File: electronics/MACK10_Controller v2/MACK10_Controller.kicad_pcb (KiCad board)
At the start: 2 copper layers, 80 x 85.7 mm, 36 parts, among them J1 Motor, J10 I/O, J3 Load Cell, J4 24V IN, J5 SSD1306, J6 INPUT, J7 E_STOP, J8 LIM_TOP, J9 LIM_BOT, U1 U1 ESP32_DEVKIT_30P, U2 HX711, U3 TMC2208, U4 LM2596 Buck Converter

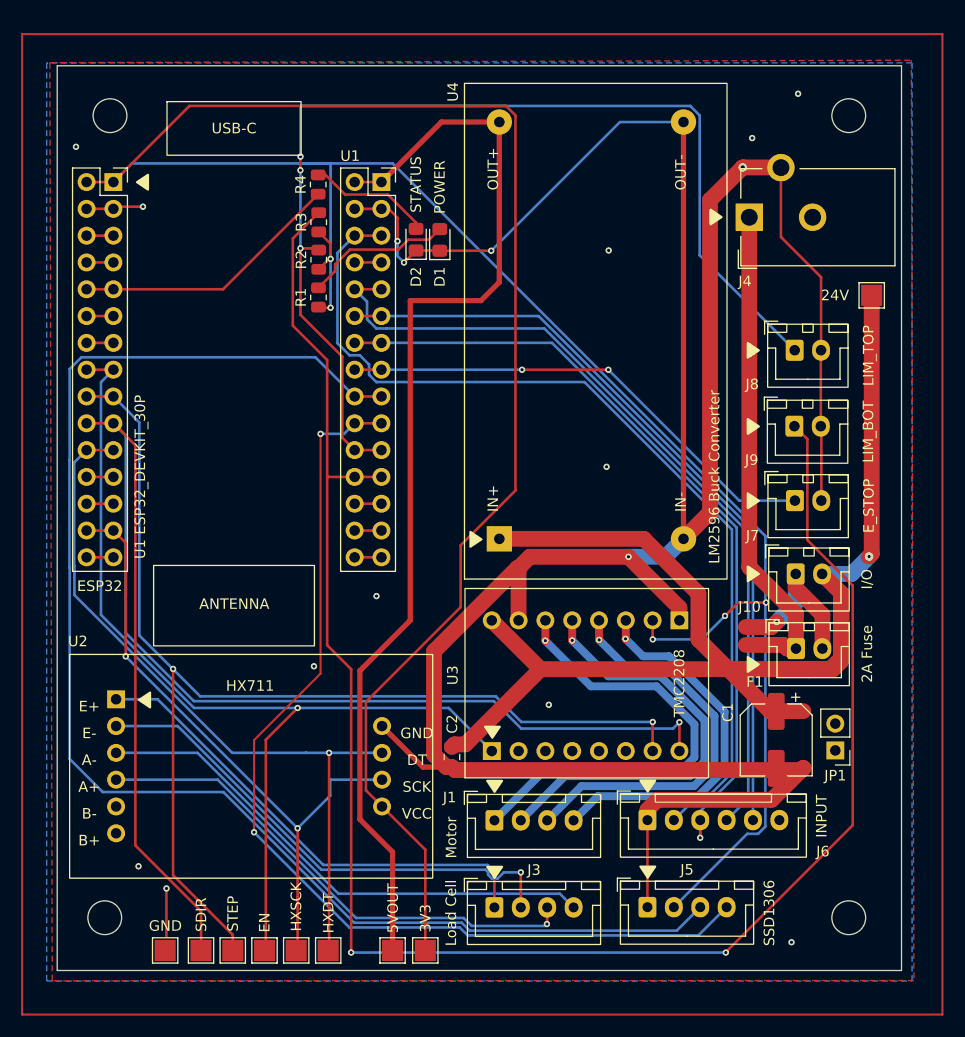
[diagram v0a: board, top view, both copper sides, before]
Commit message: First pass of PCB Layout (front and back)
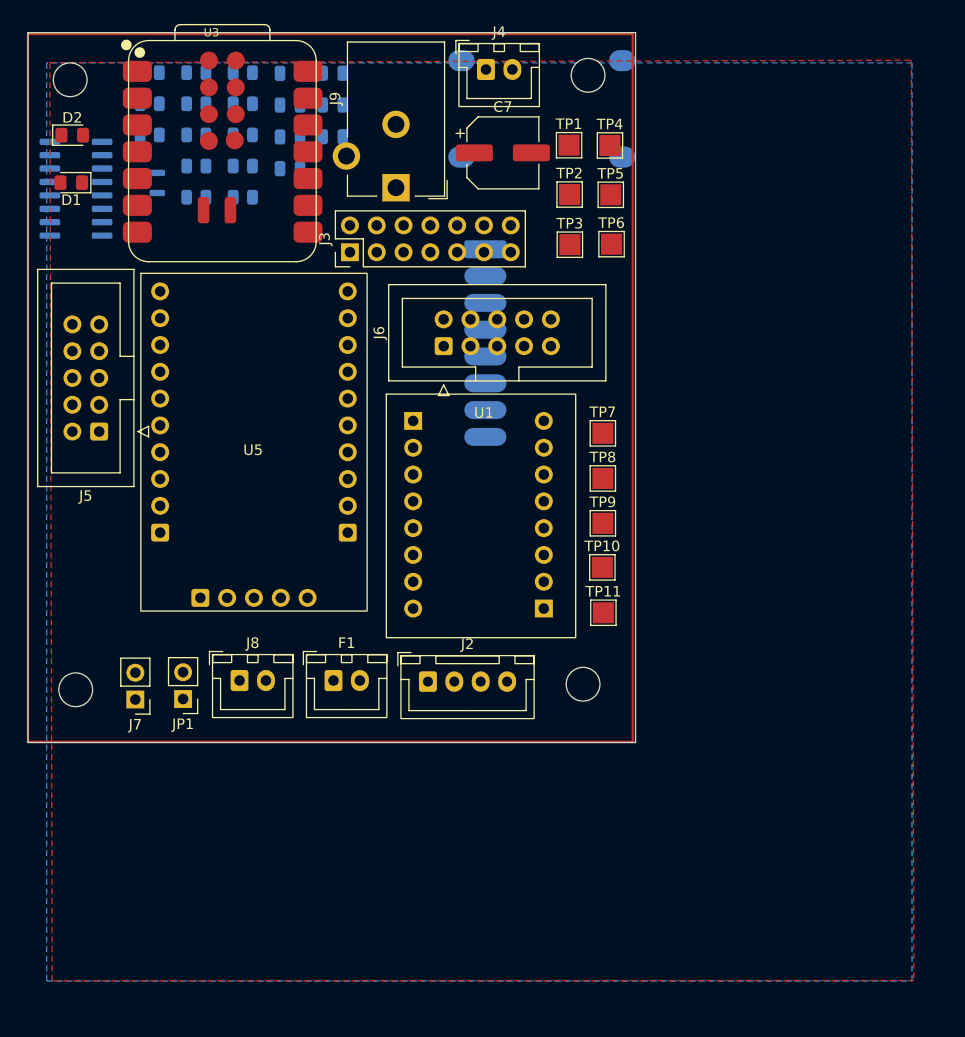
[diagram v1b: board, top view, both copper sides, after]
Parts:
- removed J1: Motor, Connector_JST:JST_XH_B4B-XH-A_1x04_P2.50mm_Vertical
- removed J10: I/O, Connector_JST:JST_XH_B2B-XH-A_1x02_P2.50mm_Vertical
- added C3: 10uF, Capacitor_SMD:C_0805_2012Metric, B.Cu at (42.1, 27.0)
- added C4: 0.1uF, Capacitor_SMD:C_0805_2012Metric, B.Cu at (42.1, 30.0)
- added C5: 100nF 50V, Capacitor_SMD:C_0805_2012Metric, B.Cu at (46.1, 21.0)
- added C6: 0.1uF, Capacitor_SMD:C_0805_2012Metric, B.Cu at (46.1, 24.0)
- added C7: 100uF 35V, Capacitor_SMD:CP_Elec_6.3x7.7, F.Cu at (62.2, 28.5)
- added C8: 0.1uF, Capacitor_SMD:C_0805_2012Metric, B.Cu at (46.1, 27.0)
- added J2: Motor, Connector_JST:JST_XH_B4B-XH-A_1x04_P2.50mm_Vertical, F.Cu at (55.1, 78.6)
- added Q1: SS8550, Package_TO_SOT_SMD:SOT-23, B.Cu at (28.5, 31.4)
- added R10: 10k, Resistor_SMD:R_0805_2012Metric, B.Cu at (33.2, 32.7)
- added R11: 4.7k, DNP, Resistor_SMD:R_0805_2012Metric, B.Cu at (28.8, 20.9)
- added R12: 4.7k, DNP, Resistor_SMD:R_0805_2012Metric, B.Cu at (28.8, 23.9)
- added R13: 10k, Resistor_SMD:R_0805_2012Metric, B.Cu at (28.8, 26.8)
- added R5: 470, Resistor_SMD:R_0805_2012Metric, B.Cu at (37.6, 32.7)
- added R6: 1k, Resistor_SMD:R_0805_2012Metric, B.Cu at (33.2, 20.9)
- added R7: 1k, Resistor_SMD:R_0805_2012Metric, B.Cu at (33.2, 23.9)
- added R8: 10k, Resistor_SMD:R_0805_2012Metric, B.Cu at (33.2, 26.8)
- added R9: 10k, Resistor_SMD:R_0805_2012Metric, B.Cu at (33.2, 29.8)
- added TP10: 5VOUT, TestPoint:TestPoint_Pad_2.0x2.0mm, F.Cu at (71.7, 67.8)
- added TP11: GND, TestPoint:TestPoint_Pad_2.0x2.0mm, F.Cu at (71.8, 72.1)
- added U5: PCF8575, MACK10:PCF8575, F.Cu at (33.6, 70.7)
- added U6: MINI360, Mini360:Mini360_step-down, B.Cu at (65.9, 24.4)
- C1: value 100uF 35V -> 0.1uF; footprint Capacitor_SMD:CP_Elec_6.3x7.7 -> Capacitor_SMD:C_0805_2012Metric; moved to B.Cu
- C2: value 100nF 50V -> 10uF; moved to B.Cu
- D2: value STATUS -> SMD_STATUS
- J3: value Load Cell -> J_Expansion; footprint Connector_JST:JST_XH_B4B-XH-A_1x04_P2.50mm_Vertical -> Connector_PinHeader_2.54mm:PinHeader_2x07_P2.54mm_Vertical
- J4: value 24V IN -> I/O; footprint Connector_BarrelJack:BarrelJack_CUI_PJ-102AH_Horizontal -> Connector_JST:JST_XH_B2B-XH-A_1x02_P2.50mm_Vertical
- J5: value SSD1306 -> Sensor IDC; footprint Connector_JST:JST_XH_B4B-XH-A_1x04_P2.50mm_Vertical -> Connector_IDC:IDC-Header_2x05_P2.54mm_Vertical
- J6: value INPUT -> Interface IDC; footprint Connector_JST:JST_XH_B6B-XH-A_1x06_P2.50mm_Vertical -> Connector_IDC:IDC-Header_2x05_P2.54mm_Vertical
- J7: value E_STOP -> Fan; footprint Connector_JST:JST_XH_B2B-XH-A_1x02_P2.50mm_Vertical -> Connector_PinHeader_2.54mm:PinHeader_1x02_P2.54mm_Vertical
- J8: value LIM_TOP -> E_STOP
- J9: value LIM_BOT -> 24V IN; footprint Connector_JST:JST_XH_B2B-XH-A_1x02_P2.50mm_Vertical -> Connector_BarrelJack:BarrelJack_CUI_PJ-102AH_Horizontal
- R1: value 1k -> 100; moved to B.Cu
- R2: value 10k -> 100; moved to B.Cu
- R3: value 10k -> 18k; moved to B.Cu
- R4: value 1k -> 7.5k; moved to B.Cu
- TP1: value 3V3 -> STEP
- TP2: value HXDT -> HX_DT
- TP3: value 5VOUT -> HX_SCK
- TP4: value GND -> SDA
- TP5: value 24V -> SCL
- TP6: value HXSCK -> VMOT
- TP7: value EN -> M24V
- TP8: value STEP -> 3V3
- TP9: value SDIR -> 24V
- U1: value U1 ESP32_DEVKIT_30P -> TMC2208; footprint MACK10:ESP32_DEVKIT_30PIN -> MACK10:TMC2208_STEPSTICK
- U2: footprint MACK10:HX711_MODULE -> Package_SO:SOIC-16_3.9x9.9mm_P1.27mm; moved to B.Cu
- U3: value TMC2208 -> XIAO-C6; footprint MACK10:TMC2208_STEPSTICK -> XIAO-SEEDSTUDIO:XIAO-ESP32-C6-SMD
- U4: value LM2596 Buck Converter -> INA226; footprint MACK10:LM2596_BUCK_CONVERTER -> MACK10:INA226; moved to B.Cu
- moved TP4 87.1 mm to (72.4, 27.8)
- moved C1 78.2 mm to (42.1, 21.0), turned to 180 degrees
- moved TP1 77.5 mm to (68.5, 27.8), turned to 0 degrees
- moved TP2 75.2 mm to (68.5, 32.5), turned to 0 degrees
- moved TP6 73.3 mm to (72.5, 37.2), turned to 0 degrees
- moved TP3 69.0 mm to (68.6, 37.2), turned to 0 degrees
- moved J5 68.8 mm to (24.0, 54.9), turned to 180 degrees
- moved J7 65.3 mm to (27.4, 80.3), turned to 180 degrees
- moved C2 63.7 mm to (42.1, 24.0), turned to 180 degrees
- moved J3 63.6 mm to (47.7, 37.9), turned to 90 degrees
- moved JP1 62.0 mm to (31.9, 80.3)
- moved J8 61.2 mm to (37.3, 78.5)
- moved TP7 58.6 mm to (71.7, 55.1), turned to 0 degrees
- moved U3 57.7 mm to (26.8, 38.9), turned to 0 degrees
- moved TP8 56.8 mm to (71.7, 59.4), turned to 0 degrees
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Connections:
- C1 pad 1: /+24V -> Net-(U2-INA-)
- C1 pad 2: /GND -> Net-(U2-INA+)
- C2 pad 1: /+24V -> /GND
- C2 pad 2: /GND -> /+5V
- D2 pad 1: /GND -> /STATUS
- J3 pad 1: /LOAD_E+ -> /GND
- J3 pad 2: /LOAD_E- -> /GND
- J3 pad 3: /LOAD_A+ -> /3V3
- J3 pad 4: /LOAD_A- -> /IO3
- J4 pad 1: /24VIN -> Net-(F1-Pin_2)
- J4 pad 2: unconnected-(J4-Pin_2-Pad2) -> /+24V
- J5 pad 1: /GND -> /E_STOP_SENSE
- J5 pad 2: /3V3 -> /GND
- J5 pad 3: /ESP32 D33 -> /LIM_BOT
- J5 pad 4: /ESP32 D32 -> /GND
- J6 pad 1: /GND -> /RIGHT
- J6 pad 2: /UP -> /LEFT
- J6 pad 3: /DOWN -> /UP
- J6 pad 4: /SELECT -> /DOWN
- J6 pad 5: /BACK -> /+5V
- J6 pad 6: unconnected-(J6-Pin_6-Pad6) -> /USER_LED
- J7 pad 1: /ESP32 D25 -> /+5V
- J8 pad 1: /ESP32 D35 -> /+24V
- J8 pad 2: /GND -> /MOTOR_24V
- J9 pad 1: /ESP32 D34 -> /24VIN
- R1 pad 1: /3V3 -> Net-(J1-A-)
- R1 pad 2: Net-(D1-A) -> Net-(U2-INA-)
- R2 pad 1: /3V3 -> Net-(J1-E-)
- R2 pad 2: /ESP32 D35 -> Net-(U2-INA+)
- R3 pad 1: /3V3 -> Net-(U2-VFB)
- R3 pad 2: /ESP32 D34 -> Net-(J1-Shield)
- R4 pad 1: /ESP32 D4 -> /GND
- R4 pad 2: Net-(D2-A) -> Net-(U2-VFB)
- TP1 pad 1: /3V3 -> /STEP
- TP3 pad 1: /+5V -> /HX711_SCK
- TP4 pad 1: /GND -> /SDA
- TP5 pad 1: /+24V -> /SCL
- TP6 pad 1: /HX711_SCK -> /MOTOR_VMOT
- TP7 pad 1: /ENABLE -> /MOTOR_24V
- TP8 pad 1: /STEP -> /3V3
- TP9 pad 1: /DIR -> /+24V
- U1 pad 1: /3V3 -> /ENABLE
- U1 pad 10: /DIR -> /GND
- U1 pad 11: /HX711_DT -> Net-(J2-Pin_1)
- U1 pad 12: unconnected-(U1-RX0-Pad12) -> Net-(J2-Pin_2)
- U1 pad 13: unconnected-(U1-TX0-Pad13) -> Net-(J2-Pin_3)
- U1 pad 14: /HX711_SCK -> Net-(J2-Pin_4)
- U1 pad 15: unconnected-(U1-D23-Pad15) -> /3V3
- U1 pad 16: /+5V -> /GND
- U1 pad 2: /GND -> unconnected-(U1-MS1-Pad2)
- U1 pad 5: /ESP32 D4 -> unconnected-(U1-PDN_UART-Pad5)
- U1 pad 7: unconnected-(U1-TX2-Pad7) -> /STEP
- U1 pad 8: /ENABLE -> /DIR
- U1 pad 9: /STEP -> /MOTOR_VMOT
- U2 pad 1: /LOAD_E+ -> /+5V
- U2 pad 10: /3V3 -> /GND
- U2 pad 2: /LOAD_E- -> Net-(Q1-B)
- U2 pad 3: /LOAD_A- -> Net-(J1-Shield)
- U2 pad 4: /LOAD_A+ -> Net-(U2-VFB)
- U2 pad 5: unconnected-(U2-B--Pad5) -> /GND
- U2 pad 6: unconnected-(U2-B+-Pad6) -> Net-(U2-VBG)
- U2 pad 7: /GND -> Net-(U2-INA-)
- U2 pad 8: /HX711_DT -> Net-(U2-INA+)
- U2 pad 9: /HX711_SCK -> /GND
- U3 pad 1: /ENABLE -> /HX711_DT
- U3 pad 10: /GND -> unconnected-(U3-D9-Pad10)
- U3 pad 11: Net-(J1-Pin_1) -> unconnected-(U3-D10-Pad11)
- U3 pad 12: Net-(J1-Pin_2) -> /3V3
- U3 pad 13: Net-(J1-Pin_3) -> /GND
- U3 pad 14: Net-(J1-Pin_4) -> /+5V
- U3 pad 15: /3V3 -> unconnected-(U3-MTDI-Pad15)
- U3 pad 16: /GND -> unconnected-(U3-MTDO-Pad16)
- U3 pad 2: unconnected-(U3-MS1-Pad2) -> /HX711_SCK
- U3 pad 3: unconnected-(U3-MS2-Pad3) -> /STEP
- U3 pad 4: unconnected-(U3-NC-Pad4) -> /DIR
- U3 pad 5: unconnected-(U3-PDN_UART-Pad5) -> /SDA
- U3 pad 6: unconnected-(U3-CLK-Pad6) -> /SCL
- U3 pad 7: /STEP -> /ENABLE
- U3 pad 8: /DIR -> /PCF_INT
- U3 pad 9: /+24V -> /RGB_STATUS
- U4 pad 1: /+24V -> /MOTOR_24V
- U4 pad 2: /GND -> /MOTOR_VMOT
- U4 pad 3: /+5V -> /MOTOR_VMOT
- U4 pad 4: /GND -> unconnected-(U4-ALE-Pad4)
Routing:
- net /GND: track 285.4 -> 0.00 mm, vias 17 -> 0
- net /3V3: track 284.2 -> 0.00 mm, vias 5 -> 0
- net /ESP32 D34: track 171.3 -> 0.00 mm, vias 2 -> 0
- net /+24V: track 141.2 -> 0.00 mm, vias 1 -> 0
- net /ESP32 D33: track 135.9 -> 0.00 mm
- net /DIR: track 135.5 -> 0.00 mm, vias 1 -> 0
- net /STEP: track 110.1 -> 0.00 mm, vias 2 -> 0
- net /+5V: track 105.2 -> 0.00 mm
- net /ESP32 D35: track 103.2 -> 0.00 mm, vias 3 -> 0
- net /ESP32 D32: track 96.5 -> 0.00 mm, vias 2 -> 0
- net /ENABLE: track 92.9 -> 0.00 mm, vias 1 -> 0
- net /UP: track 89.1 -> 0.00 mm
- net /SELECT: track 78.5 -> 0.00 mm
- net /DOWN: track 76.0 -> 0.00 mm, vias 1 -> 0
- net /BACK: track 73.6 -> 0.00 mm
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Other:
- board size 80 x 85.7 mm -> 57.6 x 67.3 mm
- board text removed: "ESP32"

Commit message: PCB Layout Finalization
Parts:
- added J10: BYP_2, Connector_PinHeader_2.54mm:PinHeader_1x02_P2.54mm_Vertical, F.Cu at (23.1, 31.0)
- D2: value SMD_STATUS -> STATUS
- F1: value 2A Fuse -> Fuse
- JP1: value FUSE_BYPASS -> BYP_1
- U2: moved to F.Cu
- moved F1 53.2 mm to (59.7, 27.1)
- moved J7 50.0 mm to (19.3, 30.9)
- moved J3 48.8 mm to (27.2, 82.2)
- moved JP1 45.7 mm to (48.2, 37.5), turned to 90 degrees
- moved C5 37.1 mm to (62.1, 54.4)
- moved R8 31.6 mm to (51.2, 52.8)
- moved C6 31.4 mm to (23.5, 45.8)
- moved C8 31.4 mm to (23.5, 48.8)
- moved C1 29.4 mm to (19.8, 40.1)
- moved C2 29.2 mm to (19.7, 42.8)
- moved C3 29.2 mm to (19.7, 45.8)
- moved C4 29.2 mm to (19.7, 48.8)
- moved D1 28.6 mm to (48.3, 40.8)
- moved R9 27.2 mm to (51.1, 50.2)
- moved R6 26.4 mm to (48.2, 42.5)
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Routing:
- net /GND: track 0.00 -> 1.27 mm
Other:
- board text added: "MACK-10 CONTROL BOARD REV-B"

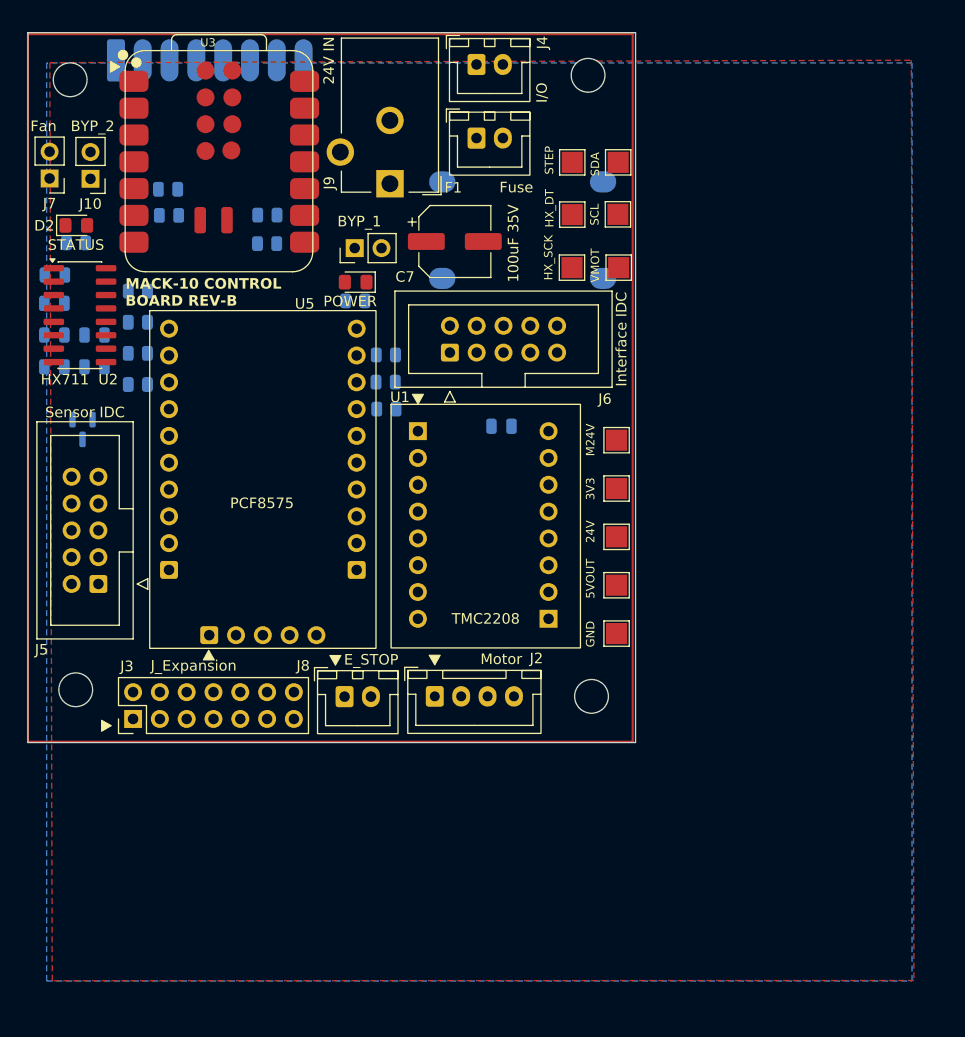
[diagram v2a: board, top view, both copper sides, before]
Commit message: Netclass and Via Updates
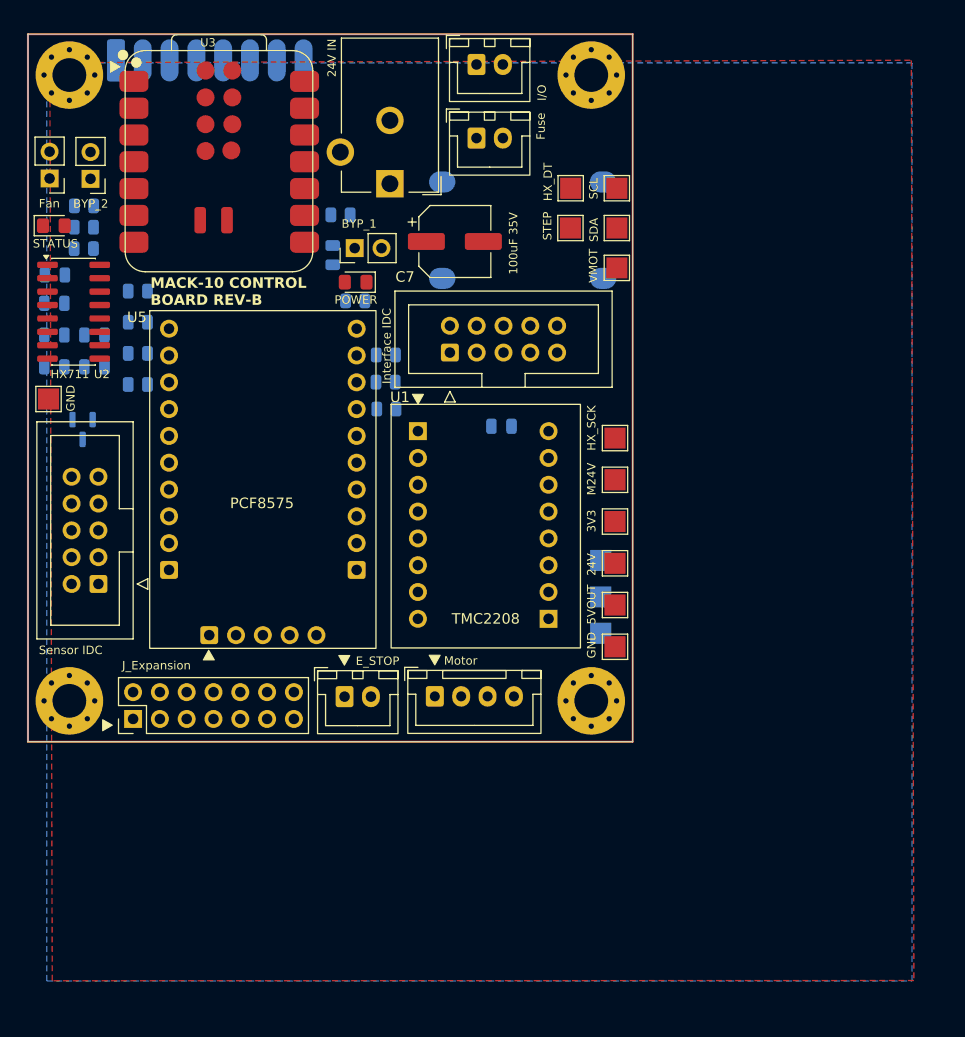
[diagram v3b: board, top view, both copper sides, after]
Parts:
- added TP10: 5VOUT, TestPoint:TestPoint_Pad_2.0x2.0mm, B.Cu at (71.5, 67.2)
- added TP11: GND, TestPoint:TestPoint_Pad_2.0x2.0mm, F.Cu at (19.2, 51.9)
- added TP11: GND, TestPoint:TestPoint_Pad_2.0x2.0mm, B.Cu at (71.5, 74.0)
- added TP8: 3V3, TestPoint:TestPoint_Pad_2.0x2.0mm, B.Cu at (71.5, 70.6)
- Mount 1: value MountingHole_3.2mm_M3 -> MountingHole_3.2mm_M3_Pad_Via; footprint MountingHole:MountingHole_3.2mm_M3 -> MountingHole:MountingHole_3.2mm_M3_Pad_Via
- Mount 2: value MountingHole_3.2mm_M3 -> MountingHole_3.2mm_M3_Pad_Via; footprint MountingHole:MountingHole_3.2mm_M3 -> MountingHole:MountingHole_3.2mm_M3_Pad_Via
- Mount 3: value MountingHole_3.2mm_M3 -> MountingHole_3.2mm_M3_Pad_Via; footprint MountingHole:MountingHole_3.2mm_M3 -> MountingHole:MountingHole_3.2mm_M3_Pad_Via
- Mount 4: value MountingHole_3.2mm_M3 -> MountingHole_3.2mm_M3_Pad_Via; footprint MountingHole:MountingHole_3.2mm_M3 -> MountingHole:MountingHole_3.2mm_M3_Pad_Via
- moved TP3 16.7 mm to (72.8, 55.5)
- moved R12 8.14 mm to (22.5, 35.6), turned to 0 degrees
- moved R11 8.12 mm to (22.5, 33.5), turned to 0 degrees
- moved R5 6.93 mm to (46.8, 34.4)
- moved R13 6.31 mm to (46.1, 38.2), turned to 90 degrees
- moved TP1 6.23 mm to (68.6, 35.6)
- moved TP4 6.23 mm to (73.0, 35.6)
- moved TP7 3.76 mm to (72.8, 59.5)
- moved TP8 3.13 mm to (72.8, 63.5)
- moved TP9 2.51 mm to (72.8, 67.4)
- moved TP2 2.50 mm to (68.7, 31.9)
- moved TP5 2.48 mm to (73.0, 31.9)
- moved D2 2.13 mm to (19.7, 35.4)
- moved TP10 1.88 mm to (72.8, 71.4)
- moved TP11 1.26 mm to (72.8, 75.3)
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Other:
- board size 57.6 x 67.3 mm -> 57.3 x 67.1 mm

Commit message: More Traces
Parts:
- moved TP8 7.27 mm to (72.8, 63.5), turned to 0 degrees
- moved TP10 4.43 mm to (72.8, 71.4), turned to 0 degrees
- moved TP11 1.86 mm to (72.8, 75.3), turned to 0 degrees
- turned R7 to 0 degrees
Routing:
- net /MOTOR_VMOT: track 0.00 -> 80.4 mm, vias 0 -> 3
- net /MOTOR_24V: track 0.00 -> 55.6 mm
- net /+5V: track 0.00 -> 41.8 mm, vias 0 -> 2
- net /ENABLE: track 0.00 -> 38.3 mm, vias 0 -> 1
- net Net-(F1-Pin_2): track 0.00 -> 24.4 mm, vias 0 -> 1
- net /24VIN: track 0.00 -> 17.5 mm
- net /+24V: track 0.00 -> 13.6 mm, vias 0 -> 1
- net /3V3: track 0.00 -> 10.0 mm, vias 0 -> 2
- net /SDA: track 0.00 -> 4.50 mm, vias 0 -> 1
- net /SCL: track 0.00 -> 4.30 mm, vias 0 -> 1

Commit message: Majority of traces done
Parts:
- moved TP11 58.9 mm to (73.0, 28.0), turned to 0 degrees
- moved TP2 52.4 mm to (20.2, 51.8)
- moved TP3 48.8 mm to (24.2, 51.8)
- moved TP9 39.7 mm to (68.6, 28.0)
- moved C2 9.05 mm to (19.7, 51.8), turned to 0 degrees
- moved C1 8.70 mm to (19.6, 48.8)
- moved C8 8.58 mm to (23.4, 40.2)
- moved R4 7.27 mm to (23.5, 44.5)
- moved C6 6.78 mm to (19.6, 40.2), turned to 0 degrees
- moved R3 6.68 mm to (23.4, 42.4)
- moved R1 6.51 mm to (23.5, 46.6)
- moved R2 5.90 mm to (23.4, 48.7)
- moved C4 3.40 mm to (19.7, 45.4)
- moved C3 3.34 mm to (19.6, 42.5), turned to 0 degrees
- moved Q1 2.74 mm to (19.7, 55.1)
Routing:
- net /3V3: track 10.0 -> 209.3 mm, vias 2 -> 9
- net /+5V: track 41.8 -> 232.6 mm, vias 2 -> 11
- net /SDA: track 4.50 -> 169.7 mm, vias 1 -> 10
- net /SCL: track 4.30 -> 165.6 mm, vias 1 -> 13
- net /STEP: track 0.00 -> 127.9 mm, vias 0 -> 4
- net /MOTOR_24V: track 55.6 -> 151.5 mm, vias 0 -> 7
- net /+24V: track 13.6 -> 82.1 mm, vias 1 -> 2
- net /DIR: track 0.00 -> 62.4 mm, vias 0 -> 5
- net /IO1: track 0.00 -> 55.3 mm
- net /IO2: track 0.00 -> 49.8 mm
- net /PCF_INT: track 0.00 -> 48.0 mm, vias 0 -> 2
- net /HX711_DT: track 0.00 -> 40.4 mm, vias 0 -> 2
- net /E_STOP_SENSE: track 0.00 -> 40.2 mm
- net /HX711_SCK: track 0.00 -> 38.0 mm, vias 0 -> 2
- net /STATUS: track 0.00 -> 37.6 mm, vias 0 -> 3
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
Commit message: DRC Cleanup - Zero Violations
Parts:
- moved C8 0.69 mm to (23.2, 39.6)
- moved U3 0.63 mm to (27.1, 39.9)
- moved TP2 0.48 mm to (20.7, 51.8)
- moved C5 0.47 mm to (62.0, 54.9)
- moved U4 0.44 mm to (35.0, 30.2)
- moved R1 0.15 mm to (23.3, 46.6)
- moved R4 0.15 mm to (23.3, 44.5)
- moved R2 0.12 mm to (23.3, 48.7)
- moved R3 0.10 mm to (23.3, 42.4)
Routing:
- net /SCL: track 165.6 -> 154.5 mm, vias 13 -> 12
- net /GND: track 29.2 -> 34.8 mm, vias 2 -> 42
- net /3V3: track 209.3 -> 214.0 mm, vias 9 -> 13
- net Net-(U2-INA-): track 10.0 -> 6.20 mm
- net /HX711_SCK: track 38.0 -> 34.5 mm
- net /ENABLE: track 40.2 -> 36.8 mm
- net Net-(U2-VFB): track 3.51 -> 6.38 mm
- net Net-(Q1-B): track 29.2 -> 31.8 mm
- net /MOTOR_VMOT: track 104.7 -> 102.2 mm, vias 3 -> 5
- net /MOTOR_24V: track 151.5 -> 153.9 mm
- net /STEP: track 127.9 -> 130.1 mm
- net /DIR: track 62.4 -> 61.8 mm
- net /HX711_DT: track 40.4 -> 40.7 mm, vias 2 -> 4
- net Net-(J1-Shield): track 19.9 -> 20.3 mm, vias 2 -> 1
- net Net-(U2-INA+): track 4.93 -> 4.77 mm, vias 2 -> 1
